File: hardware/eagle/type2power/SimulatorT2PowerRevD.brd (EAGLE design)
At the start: 48.3 x 48.3 mm, 8 parts

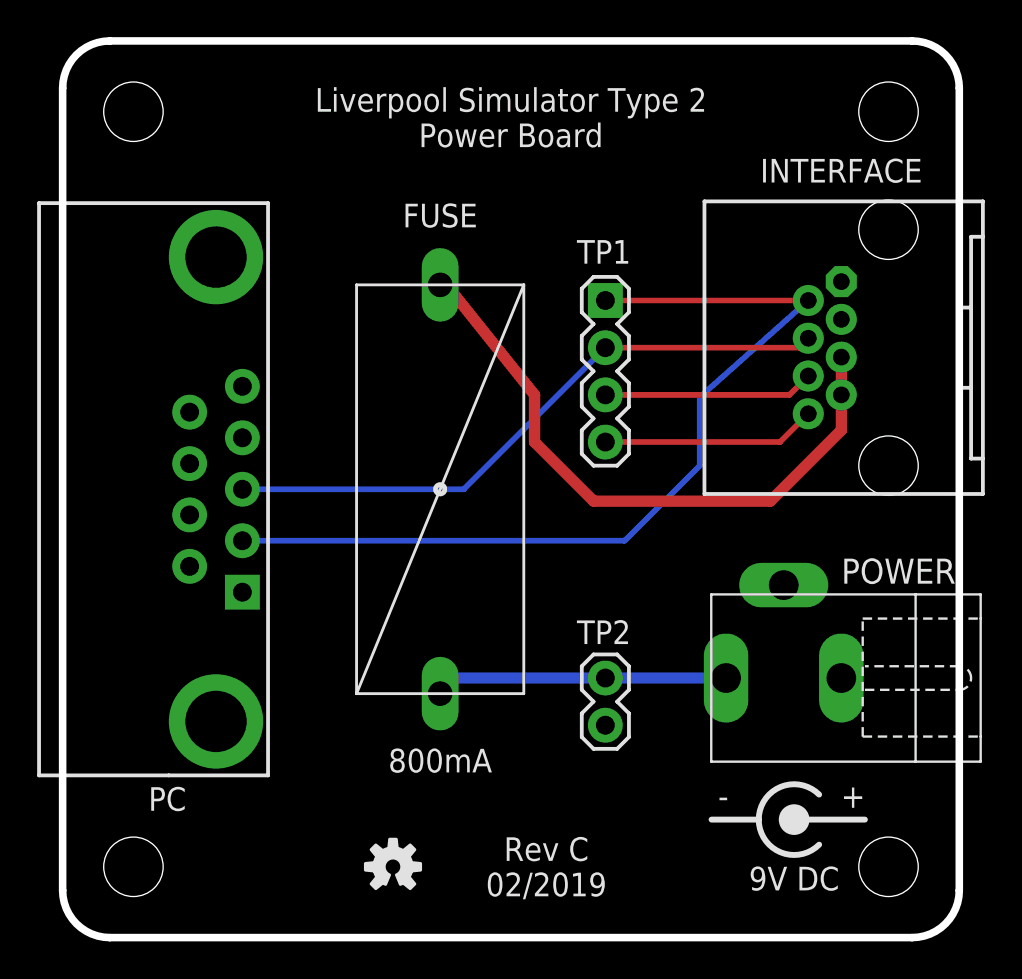
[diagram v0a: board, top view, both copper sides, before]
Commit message: Enhanced surge protection
Power Rev D, 2nd PC Rev B boards with improved surge protection,
Gerbers, Cost Estimation tool, New enclosure drilling templates.
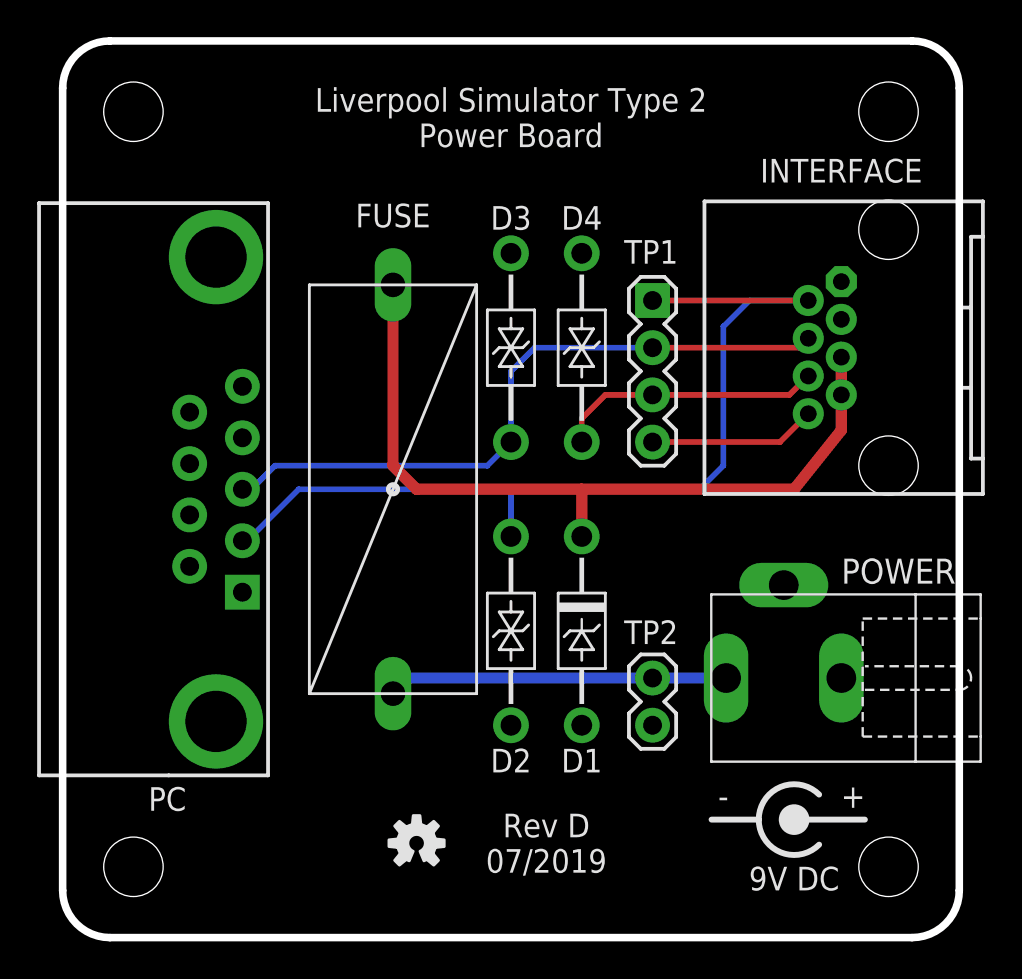
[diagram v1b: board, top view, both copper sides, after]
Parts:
- added D1: SA12A, AIC_Custom:DO41_TVS_UNI
- added D2, D3, D4: SA15CA, AIC_Custom:DO41_TVS_BI
- moved FUSE 2.54 mm to (17.8, 24.1)
- moved TP1 2.54 mm to (31.8, 34.3)
- moved TP2 2.54 mm to (31.8, 14.0)
- moved LOGO1 1.80 mm to (19.1, 5.08)
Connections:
- net GND: now also D1.ANODE, D2.A, D3.A, D4.A
- net RXD: now also D3.C
- net TX2: now also D4.C
- net TXD: now also D2.C
- net VIN2: now also D1.CATHODE
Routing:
- net VIN2: track 34.4 -> 42.4 mm
- net TX2: track 11.3 -> 14.4 mm
- net P8: track 11.6 -> 9.01 mm
- net TXD: track 48.7 -> 51.1 mm
- net VIN: track 15.9 -> 18.3 mm
- net RXD: track 33.8 -> 36.1 mm
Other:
- board text added: "Rev D 07/2019"
- board text removed: "Rev C 02/2019"
